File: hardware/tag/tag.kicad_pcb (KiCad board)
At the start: 2 copper layers, 98.2 x 48.3 mm, 16 parts

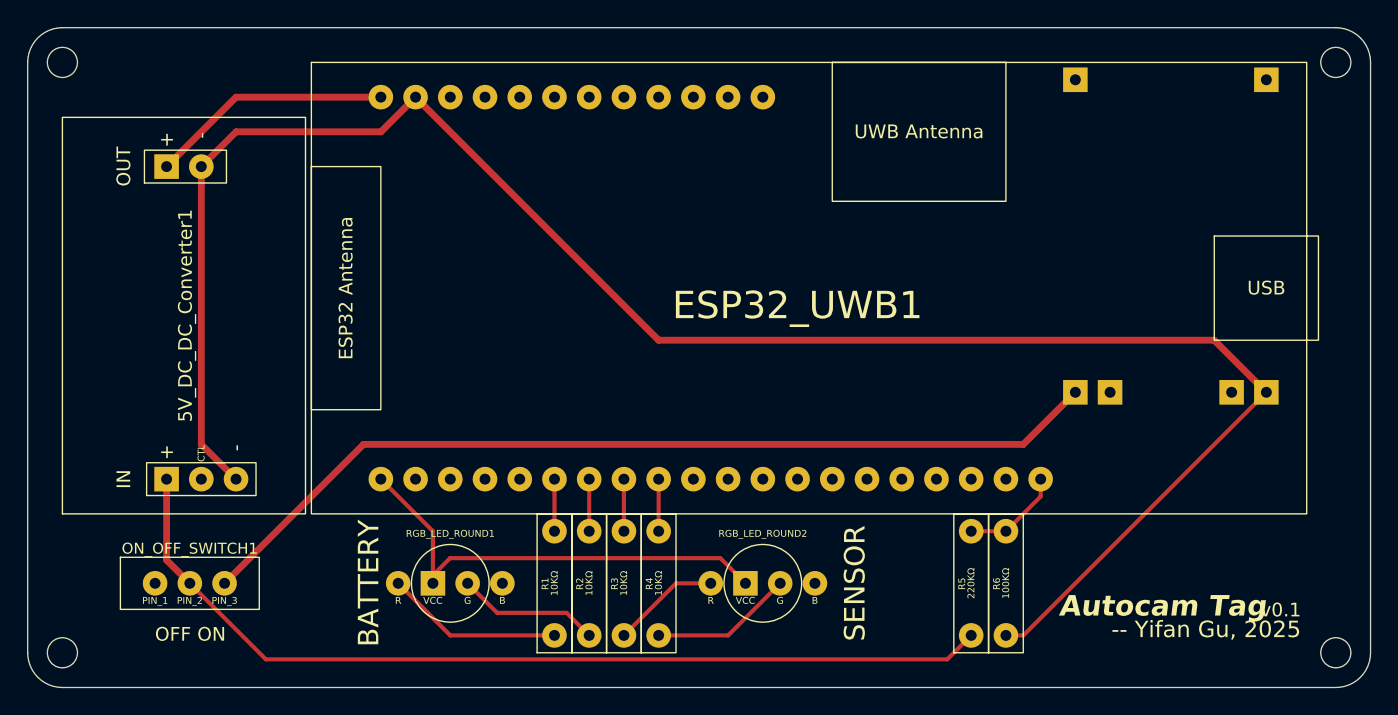
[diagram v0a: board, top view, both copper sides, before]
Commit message: hardware: Update pcd design for better wiring clearance.
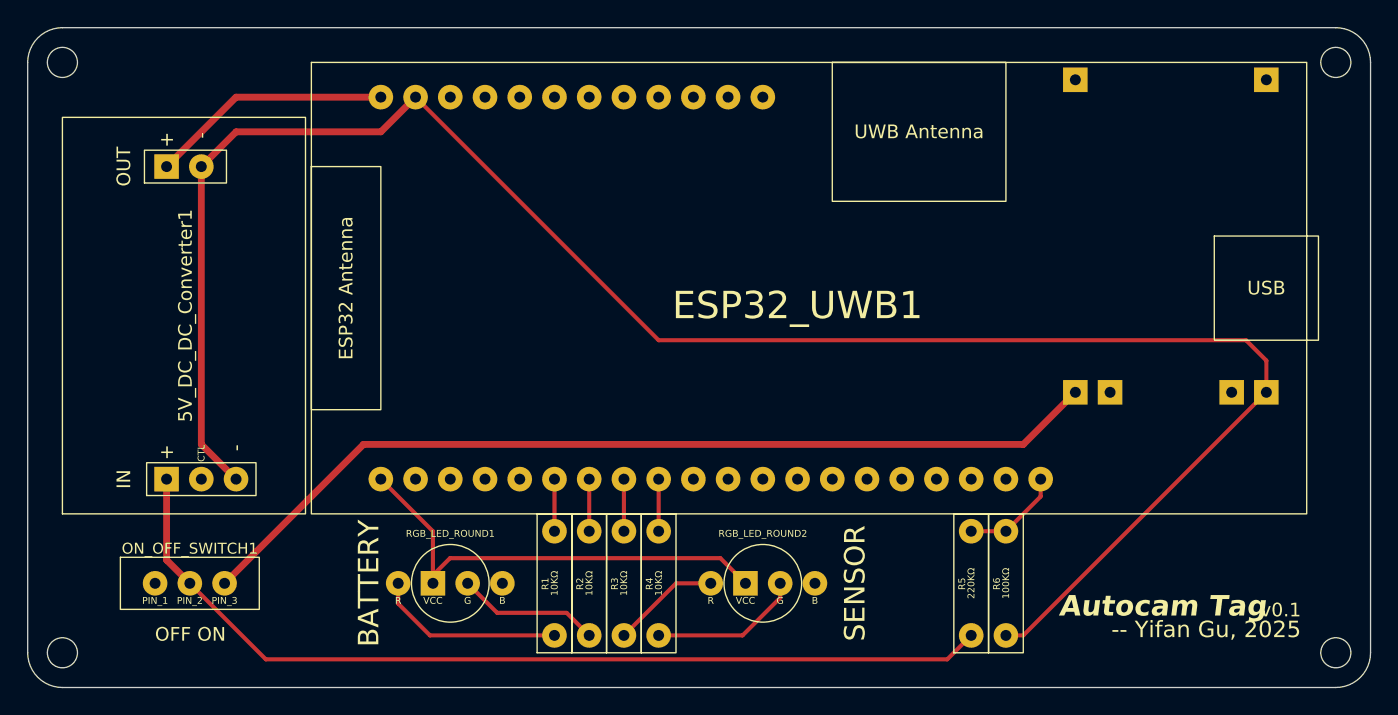
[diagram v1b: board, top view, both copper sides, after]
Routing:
- net Net-(Battery_Charger1-OUT-): track 139.3 -> 140.6 mm
- net Net-(RGB_LED_ROUND1-R): track 13.0 -> 13.9 mm
- net Net-(RGB_LED_ROUND2-G): track 10.5 -> 11.1 mm
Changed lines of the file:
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@@
 	)
 	(segment
-		(start 45.935 59.69)
-		(end 53.555 59.69)
+		(start 53.555 59.69)
+		(end 44.45 59.69)
 		(width 0.3)
 		(layer "F.Cu")
@@
 	)
 	(segment
-		(start 42.125 55.88)
-		(end 45.935 59.69)
+		(start 44.45 59.69)
+		(end 42.125 57.365)
+		(width 0.3)
+		(layer "F.Cu")
+		(net 33)
+	)
+	(segment
+		(start 42.125 57.365)
+		(end 42.125 55.88)
 		(width 0.3)
 		(layer "F.Cu")
@@
 	)
 	(segment
-		(start 66.255 59.69)
+		(start 70.065 56.935)
 		(end 70.065 55.88)
 		(width 0.3)
@@
 	(segment
 		(start 61.175 59.69)
-		(end 66.255 59.69)
+		(end 67.31 59.69)
+		(width 0.3)
+		(layer "F.Cu")
+		(net 36)
+	)
+	(segment
+		(start 67.31 59.69)
+		(end 70.065 56.935)
 		(width 0.3)
 		(layer "F.Cu")
@@
 	)
 	(segment
-		(start 105.625 41.91)
-		(end 101.815 38.1)
-		(width 0.5)
-		(layer "F.Cu")
-		(net 45)
-	)
-	(segment
 		(start 105.625 41.912792)
 		(end 105.625 41.91)
@@
 	)
 	(segment
-		(start 61.175 38.1)
-		(end 43.395 20.32)
-		(width 0.5)
+		(start 105.625 41.91)
+		(end 105.625 39.585)
+		(width 0.3)
 		(layer "F.Cu")
 		(net 45)
@@
 	)
 	(segment
-		(start 101.815 38.1)
+		(start 104.14 38.1)
 		(end 61.175 38.1)
-		(width 0.5)
+		(width 0.3)
 		(layer "F.Cu")
 		(net 45)
@@
 	)
 	(segment
+		(start 105.625 39.585)
+		(end 104.14 38.1)
+		(width 0.3)
+		(layer "F.Cu")
+		(net 45)
+	)
+	(segment
 		(start 87.845 59.69)
 		(end 86.575 59.69)
@@
 		(width 0.3)
 		(layer "F.Cu")
+		(net 45)
+	)
+	(segment
+		(start 61.175 38.1)
+		(end 43.395 20.32)
+		(width 0.3)
+		(layer "F.Cu")
